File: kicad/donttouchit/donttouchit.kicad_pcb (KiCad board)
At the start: 2 copper layers, 40 x 61 mm, 46 parts, among them J1 Conn_01x02_Female, J10 Conn_01x04_Male, J2 Conn_01x02_Female, J3 Conn_01x02_Female, J4 Conn_01x02_Female, J5 Conn_01x02_Female, J6 Conn_01x02_Female, J7 Conn_01x02_Female, J8 Conn_01x02_Female, J9 Conn_01x02_Female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

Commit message: i2c pull up resistors added
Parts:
- added R1: 2k2, Resistor_SMD:R_0603_1608Metric_Pad0.98x0.95mm_HandSolder, F.Cu at (138.4, 77.3)
- added R2: 2k2, Resistor_SMD:R_0603_1608Metric_Pad0.98x0.95mm_HandSolder, F.Cu at (136.7, 77.3)
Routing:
- net Net-(J10-Pad2): track 3.26 -> 8.86 mm
- net VCC: track 19.9 -> 23.2 mm
- net Net-(J10-Pad3): track 16.9 -> 20.1 mm, vias 1 -> 2
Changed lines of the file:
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@@
   (net 7 "IN2B")
   (net 8 "IN2A")
-  (net 9 "Net-(U1-Pad5)")
+  (net 9 "Net-(TP15-Pad1)")
   (net 10 "Net-(U1-Pad3)")
   (net 11 "IN3B")
@@
       (net 2 "GND") (pinfunction "ADDR") (pintype "input"))
     (pad "5" smd roundrect (at -0.75 1.9375) (size 0.25 0.875) (layers "F.Cu" "F.Paste" "F.Mask") (roundrect_rratio 0.25)
-      (net 9 "Net-(U1-Pad5)") (pinfunction "INTB") (pintype "open_collector"))
+      (net 9 "Net-(TP15-Pad1)") (pinfunction "INTB") (pintype "open_collector"))
     (pad "6" smd roundrect (at -0.25 1.9375) (size 0.25 0.875) (layers "F.Cu" "F.Paste" "F.Mask") (roundrect_rratio 0.25)
       (net 2 "GND") (pinfunction "SD") (pintype "input"))
@@
       (net 11 "IN3B") (pinfunction "1") (pintype "passive"))
   )
+  (footprint "Resistor_SMD:R_0603_1608Metric_Pad0.98x0.95mm_HandSolder" (layer "F.Cu")
+    (at 136.7 77.3 90)
+    (descr "Resistor SMD 0603 (1608 Metric), square (rectangular) end terminal, IPC_7351 nominal with elongated pad for handsoldering. (Body size source: IPC-SM-782 page 72, https://www.pcb-3d.com/wordpress/wp-content/uploads/ipc-sm-782a_amendment_1_and_2.pdf), generated with kicad-footprint-generator")
+    (tags "resistor handsolder")
+    (property "Sheetfile" "donttouchit.kicad_sch")
+    (property "Sheetname" "")
+    (attr smd)
+    (fp_text reference "R2" (at 0 -1.43 90) (layer "F.SilkS")
+      (effects (font (size 1 1) (thickness 0.15)))
+    )
+    (fp_text value "2k2" (at 0 1.43 90) (layer "F.Fab")
+      (effects (font (size 1 1) (thickness 0.15)))
+    )
+    (fp_text user "${REFERENCE}" (at 0 0 90) (layer "F.Fab")
+      (effects (font (size 0.4 0.4) (thickness 0.06)))
+    )
+    (fp_line (start -0.254724 0.5225) (end 0.254724 0.5225) (layer "F.SilkS") (width 0.12))
+    (fp_line (start -0.254724 -0.5225) (end 0.254724 -0.5225) (layer "F.SilkS") (width 0.12))
+    (fp_line (start 1.65 -0.73) (end 1.65 0.73) (layer "F.CrtYd") (width 0.05))
+    (fp_line (start 1.65 0.73) (end -1.65 0.73) (layer "F.CrtYd") (width 0.05))
+    (fp_line (start -1.65 -0.73) (end 1.65 -0.73) (layer "F.CrtYd") (width 0.05))
+    (fp_line (start -1.65 0.73) (end -1.65 -0.73) (layer "F.CrtYd") (width 0.05))
+    (fp_line (start -0.8 -0.4125) (end 0.8 -0.4125) (layer "F.Fab") (width 0.1))
+    (fp_line (start 0.8 -0.4125) (end 0.8 0.4125) (layer "F.Fab") (width 0.1))
+    (fp_line (start -0.8 0.4125) (end -0.8 -0.4125) (layer "F.Fab") (width 0.1))
+    (fp_line (start 0.8 0.4125) (end -0.8 0.4125) (layer "F.Fab") (width 0.1))
+    (pad "1" smd roundrect (at -0.9125 0 90) (size 0.975 0.95) (layers "F.Cu" "F.Paste" "F.Mask") (roundrect_rratio 0.25)
+      (net 1 "VCC") (pintype "passive"))
+    (pad "2" smd roundrect (at 0.9125 0 90) (size 0.975 0.95) (layers "F.Cu" "F.Paste" "F.Mask") (roundrect_rratio 0.25)
+      (net 14 "Net-(J10-Pad3)") (pintype "passive"))
+    (model "${KICAD6_3DMODEL_DIR}/Resistor_SMD.3dshapes/R_0603_1608Metric.wrl"
+      (offset (xyz 0 0 0))
+      (scale (xyz 1 1 1))
+      (rotate (xyz 0 0 0))
+    )
+  )
   (footprint "TestPoint:TestPoint_THTPad_1.5x1.5mm_Drill0.7mm" (layer "F.Cu")
     (at 143 77)
@@
     (pad "1" thru_hole rect (at 0 0) (size 1.5 1.5) (drill 0.7) (layers *.Cu *.Mask)
       (net 3 "IN0B") (pinfunction "1") (pintype "passive"))
+  )
+  (footprint "Resistor_SMD:R_0603_1608Metric_Pad0.98x0.95mm_HandSolder" (layer "F.Cu")
+    (at 138.4 77.3 90)
+    (descr "Resistor SMD 0603 (1608 Metric), square (rectangular) end terminal, IPC_7351 nominal with elongated pad for handsoldering. (Body size source: IPC-SM-782 page 72, https://www.pcb-3d.com/wordpress/wp-content/uploads/ipc-sm-782a_amendment_1_and_2.pdf), generated with kicad-footprint-generator")
+    (tags "resistor handsolder")
+    (property "Sheetfile" "donttouchit.kicad_sch")
+    (property "Sheetname" "")
+    (attr smd)
+    (fp_text reference "R1" (at 0 -1.43 90) (layer "F.SilkS")
+      (effects (font (size 1 1) (thickness 0.15)))
+    )
+    (fp_text value "2k2" (at 0 1.43 90) (layer "F.Fab")
+      (effects (font (size 1 1) (thickness 0.15)))
+    )
+    (fp_text user "${REFERENCE}" (at 0 0 90) (layer "F.Fab")
+      (effects (font (size 0.4 0.4) (thickness 0.06)))
+    )
+    (fp_line (start -0.254724 0.5225) (end 0.254724 0.5225) (layer "F.SilkS") (width 0.12))
+    (fp_line (start -0.254724 -0.5225) (end 0.254724 -0.5225) (layer "F.SilkS") (width 0.12))
+    (fp_line (start -1.65 0.73) (end -1.65 -0.73) (layer "F.CrtYd") (width 0.05))
+    (fp_line (start -1.65 -0.73) (end 1.65 -0.73) (layer "F.CrtYd") (width 0.05))
+    (fp_line (start 1.65 -0.73) (end 1.65 0.73) (layer "F.CrtYd") (width 0.05))
+    (fp_line (start 1.65 0.73) (end -1.65 0.73) (layer "F.CrtYd") (width 0.05))
+    (fp_line (start 0.8 -0.4125) (end 0.8 0.4125) (layer "F.Fab") (width 0.1))
+    (fp_line (start -0.8 0.4125) (end -0.8 -0.4125) (layer "F.Fab") (width 0.1))
+    (fp_line (start 0.8 0.4125) (end -0.8 0.4125) (layer "F.Fab") (width 0.1))
+    (fp_line (start -0.8 -0.4125) (end 0.8 -0.4125) (layer "F.Fab") (width 0.1))
+    (pad "1" smd roundrect (at -0.9125 0 90) (size 0.975 0.95) (layers "F.Cu" "F.Paste" "F.Mask") (roundrect_rratio 0.25)
+      (net 1 "VCC") (pintype "passive"))
+    (pad "2" smd roundrect (at 0.9125 0 90) (size 0.975 0.95) (layers "F.Cu" "F.Paste" "F.Mask") (roundrect_rratio 0.25)
+      (net 13 "Net-(J10-Pad2)") (pintype "passive"))
+    (model "${KICAD6_3DMODEL_DIR}/Resistor_SMD.3dshapes/R_0603_1608Metric.wrl"
+      (offset (xyz 0 0 0))
+      (scale (xyz 1 1 1))
+      (rotate (xyz 0 0 0))
+    )
   )
   (footprint "TestPoint:TestPoint_THTPad_1.5x1.5mm_Drill0.7mm" (layer "F.Cu")
@@
     (fp_line (start 1.25 -1.25) (end 1.25 1.25) (layer "B.CrtYd") (width 0.05))
     (pad "1" thru_hole rect (at 0 0 180) (size 1.5 1.5) (drill 0.7) (layers *.Cu *.Mask)
-      (net 9 "Net-(U1-Pad5)") (pinfunction "1") (pintype "passive"))
+      (net 9 "Net-(TP15-Pad1)") (pinfunction "1") (pintype "passive"))
   )
   (footprint "Library:PCBConnPads" (layer "B.Cu")
@@
   (segment (start 136.75 83) (end 136.75 81) (width 0.5) (layer "F.Cu") (net 1))
   (segment (start 137.5 80.25) (end 137.5 80.75) (width 0.5) (layer "F.Cu") (net 1))
+  (segment (start 138.4 78.2125) (end 136.7 78.2125) (width 0.5) (layer "F.Cu") (net 1))
   (segment (start 138.325 82.975) (end 136.775 82.975) (width 0.127) (layer "F.Cu") (net 1))
+  (segment (start 138.3875 79.75) (end 138.3875 78.225) (width 0.5) (layer "F.Cu") (net 1))
   (segment (start 144.1 82.7875) (end 144.1 84.2375) (width 0.25) (layer "F.Cu") (net 1))
+  (segment (start 138.3875 78.225) (end 138.4 78.2125) (width 0.5) (layer "F.Cu") (net 1))
   (segment (start 142.75 84.3875) (end 144.25 84.3875) (width 0.5) (layer "F.Cu") (net 1))
   (segment (start 137.5 80.75) (end 138.25 80.75) (width 0.5) (layer "F.Cu") (net 1))
@@
   (segment (start 143.6 78.9125) (end 143.6 77.6) (width 0.25) (layer "F.Cu") (net 12))
   (segment (start 141.1 80.6) (end 141 80.5) (width 0.25) (layer "F.Cu") (net 13))
+  (segment (start 139.2 78.1) (end 139.2 77.1875) (width 0.25) (layer "F.Cu") (net 13))
+  (segment (start 140.2 78.4) (end 139.5 78.4) (width 0.25) (layer "F.Cu") (net 13))
+  (segment (start 141 80.5) (end 141 79.2) (width 0.25) (layer "F.Cu") (net 13))
   (segment (start 141.9125 80.6) (end 141.1 80.6) (width 0.25) (layer "F.Cu") (net 13))
+  (segment (start 139.5 78.4) (end 139.2 78.1) (width 0.25) (layer "F.Cu") (net 13))
+  (segment (start 141 79.2) (end 140.2 78.4) (width 0.25) (layer "F.Cu") (net 13))
+  (segment (start 139.2 77.1875) (end 138.4 76.3875) (width 0.25) (layer "F.Cu") (net 13))
   (via (at 141 80.5) (size 0.6) (drill 0.3) (layers "F.Cu" "B.Cu") (free) (net 13))
   (segment (start 141 80.5) (end 140.25 81.25) (width 0.25) (layer "B.Cu") (net 13))
   (segment (start 140.25 81.25) (end 139 81.25) (width 0.25) (layer "B.Cu") (net 13))
   (segment (start 141.9125 80.1) (end 141.9125 79.3375) (width 0.25) (layer "F.Cu") (net 14))
+  (segment (start 135.25 77.8375) (end 136.7 76.3875) (width 0.25) (layer "F.Cu") (net 14))
+  (segment (start 135.25 79) (end 135.25 77.8375) (width 0.25) (layer "F.Cu") (net 14))
   (segment (start 141.9125 79.3375) (end 142.25 79) (width 0.25) (layer "F.Cu") (net 14))
+  (via (at 135.25 79) (size 0.6) (drill 0.3) (layers "F.Cu" "B.Cu") (net 14))
   (via (at 142.25 79) (size 0.6) (drill 0.3) (layers "F.Cu" "B.Cu") (free) (net 14))
   (segment (start 135.25 82.75) (end 135.75 83.25) (width 0.25) (layer "B.Cu") (net 14))

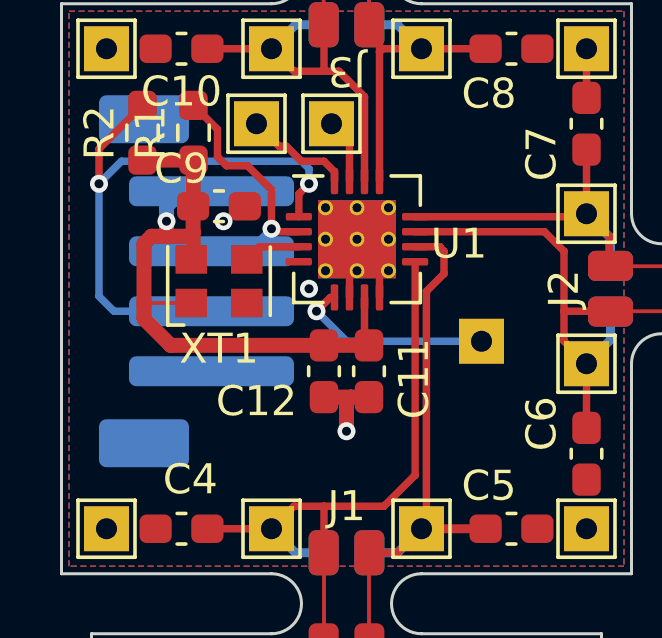
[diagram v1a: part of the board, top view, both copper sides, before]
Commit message: temperature sensor added
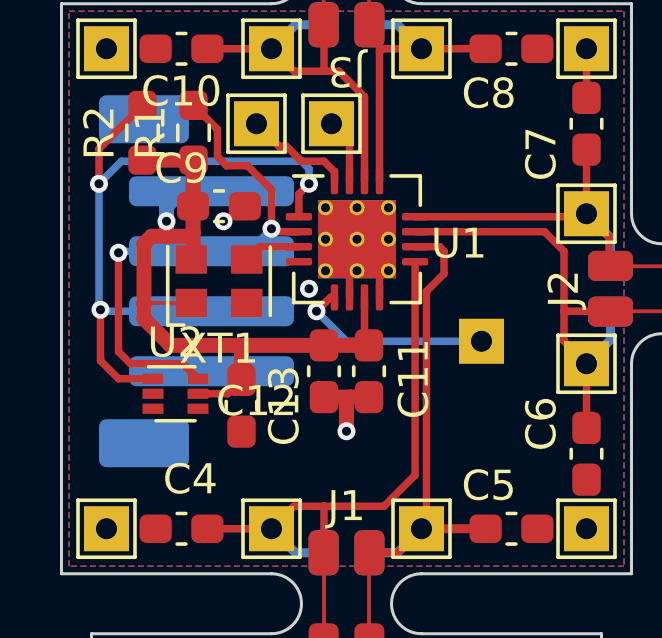
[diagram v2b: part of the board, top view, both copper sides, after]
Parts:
- added C13: 100n, Capacitor_SMD:C_0603_1608Metric_Pad1.08x0.95mm_HandSolder, F.Cu at (140.0, 86.4)
- added U2: TMP112xxDRL, Package_TO_SOT_SMD:SOT-563, F.Cu at (137.8, 86.0)
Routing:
- net Net-(J10-Pin_2): track 8.86 -> 18.3 mm, vias 1 -> 2
- net Net-(J10-Pin_3): track 20.1 -> 24.0 mm, vias 2 -> 3
- net VCC: track 23.2 -> 26.0 mm

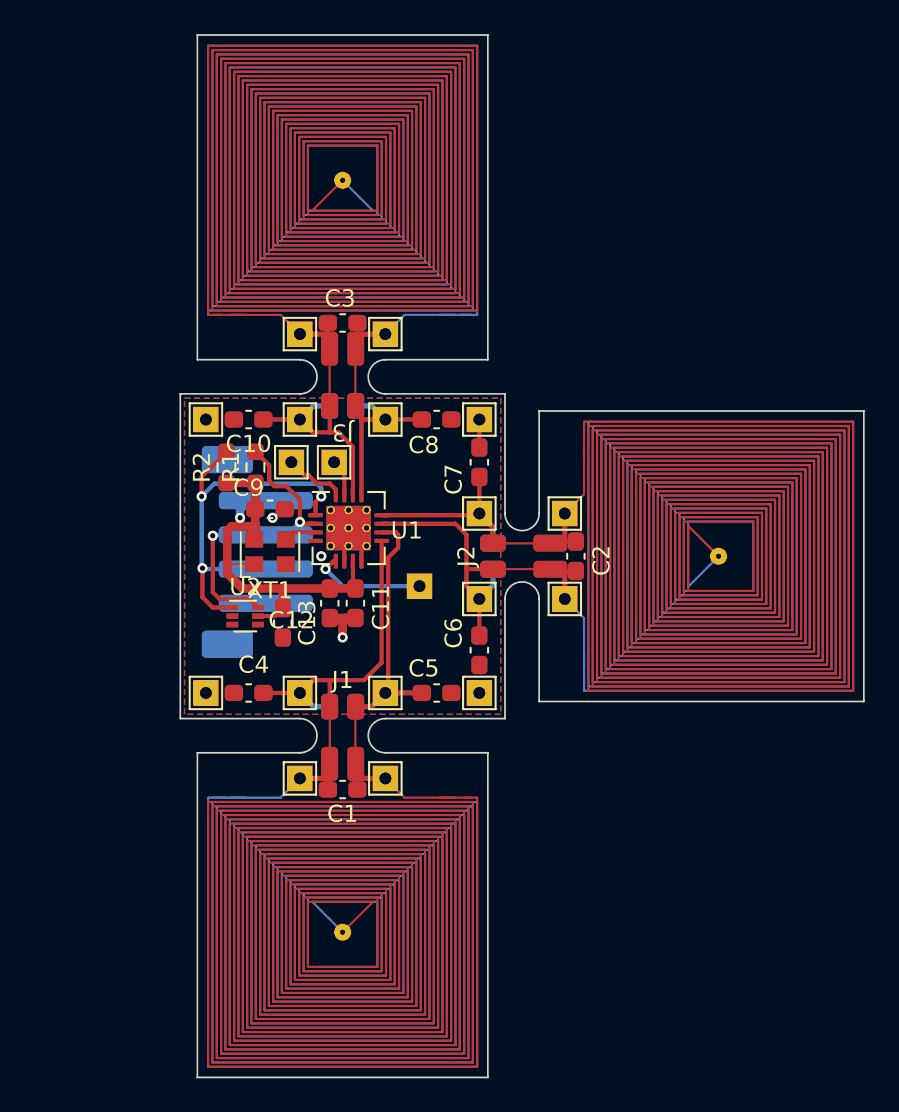
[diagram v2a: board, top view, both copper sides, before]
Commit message: I2C address solderbridges added / mounting hole added / size reduced for control section
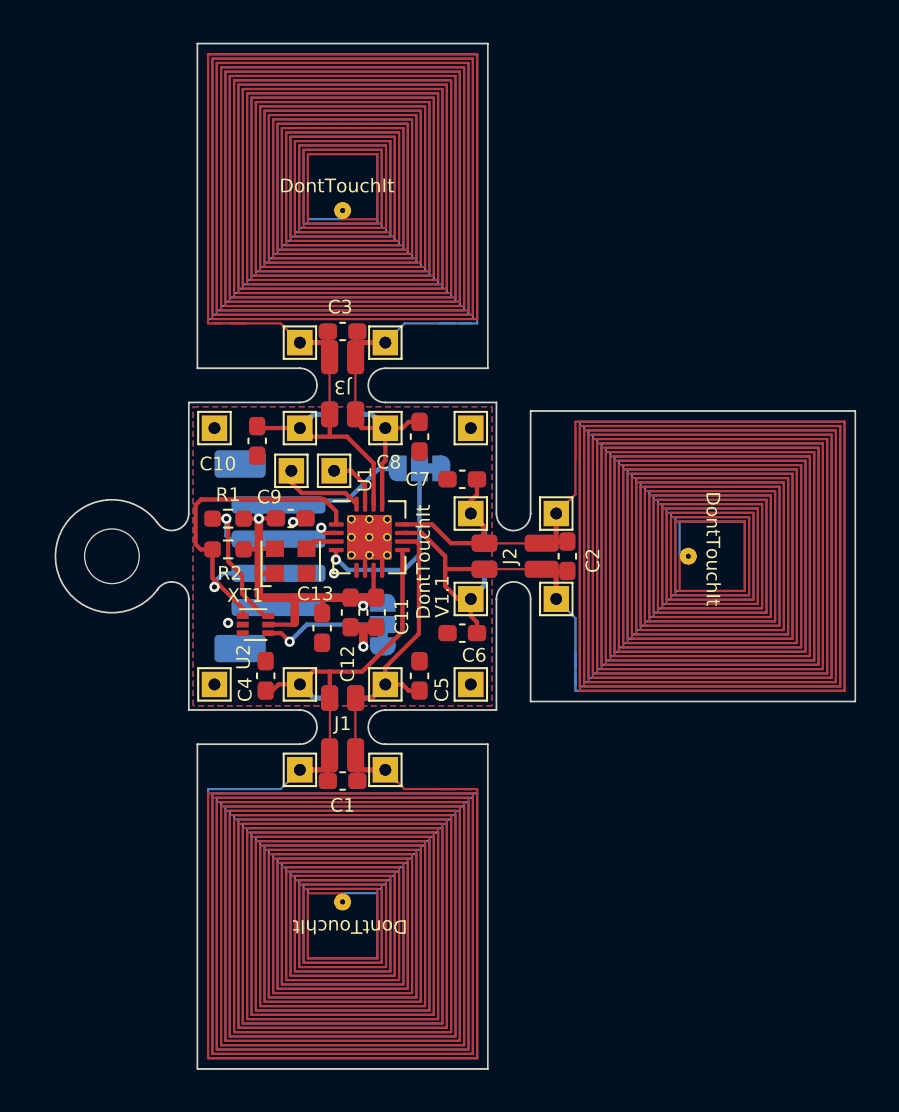
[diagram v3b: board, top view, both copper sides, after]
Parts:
- removed TP15: TestPoint, TestPoint:TestPoint_THTPad_1.5x1.5mm_Drill0.7mm
- added H1: MountingHole, MountingHole:MountingHole_3.2mm_M3, F.Cu at (126.8, 82.6)
- added JP1: I2C Adress Select, Jumper:SolderJumper-3_P1.3mm_Bridged12_RoundedPad1.0x1.5mm, B.Cu at (145.8, 86.5)
- added JP2: I2C Adress Select, Jumper:SolderJumper-3_P1.3mm_Bridged12_RoundedPad1.0x1.5mm, B.Cu at (148.0, 77.4)
- moved R2 4.80 mm to (136.8, 82.1), turned to 180 degrees
- moved R1 3.40 mm to (136.8, 80.3), turned to 180 degrees
- moved C13 2.32 mm to (142.3, 86.7)
- moved C4 1.41 mm to (139.0, 89.5), turned to 90 degrees
- moved C5 1.41 mm to (148.0, 89.5), turned to 90 degrees
- moved C6 1.41 mm to (150.5, 87.0), turned to 180 degrees
- moved C7 1.41 mm to (150.5, 78.0), turned to 180 degrees
- moved C8 1.41 mm to (148.0, 75.5), turned to -90 degrees
- moved C10 1.35 mm to (138.5, 75.8), turned to -90 degrees
- moved U1 1.33 mm to (145.1, 81.4)
- moved C11 1.33 mm to (145.5, 85.8)
- moved C12 1.33 mm to (144.0, 85.8)
- moved C9 1.33 mm to (140.5, 80.3)
- moved XT1 1.33 mm to (140.5, 82.8)
- moved J10 0.79 mm to (139.2, 82.5)
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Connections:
- U1 pad 4: GND -> Net-(JP2-C)
- U1 pad 5: Net-(U1-INTB) -> unconnected-(U1-INTB-Pad5)
- U2 pad 4: GND -> Net-(JP1-C)
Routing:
- net Net-(JP2-C): track 0.00 -> 11.1 mm, vias 0 -> 1
- net Net-(JP1-C): track 0.00 -> 7.31 mm, vias 0 -> 1
- net VCC: track 26.0 -> 33.1 mm, vias 1 -> 2
- net Net-(U1-INTB): track 6.71 -> 0.00 mm, vias 1 -> 0
- net Net-(J10-Pin_2): track 18.3 -> 15.6 mm
- net Net-(J10-Pin_3): track 24.0 -> 22.0 mm, vias 3 -> 1
- net IN1A: track 27.1 -> 25.2 mm
- net GND: track 8.76 -> 7.12 mm, vias 3 -> 4
- net IN3B: track 3.58 -> 5.03 mm
- net IN2B: track 25.0 -> 26.1 mm
- net IN3A: track 2.16 -> 3.29 mm
- net IN0A: track 30.6 -> 30.0 mm
- net IN0B: track 28.3 -> 27.8 mm
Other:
- board size 40 x 61 mm -> 46.8 x 60 mm
- board text added: "0x2A"
- board text added: "0x2B"
- board text added: "0x48"
- board text added: "0x49"
- board text added: "3V3"
- board text added: "DontTouchIt"
- board text added: "Gnd"
- board text added: "LDC"
- board text added: "SCL"
- board text added: "SDA"
- board text added: "Temp"
- board text added: "V1.1"

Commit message: smaller formfactor that fits in the space of an Omron probe, 4th sensor pads removed
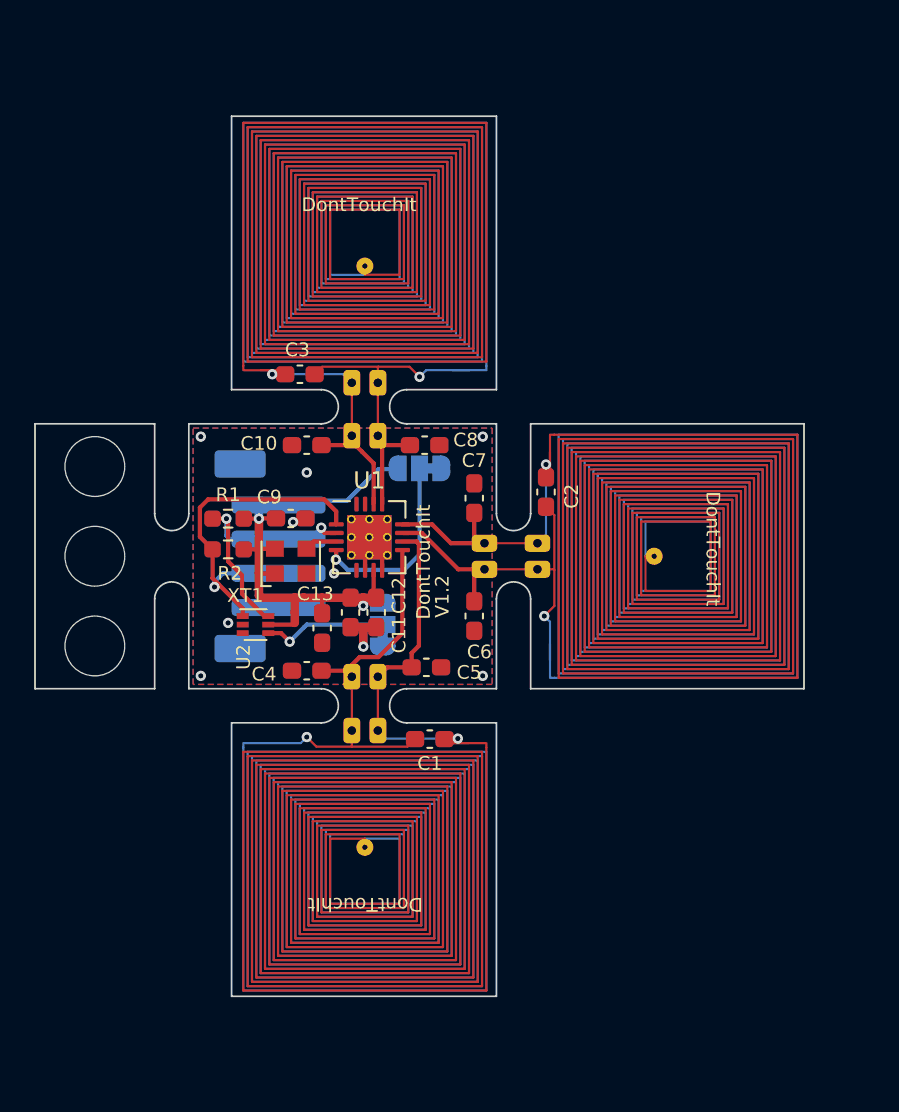
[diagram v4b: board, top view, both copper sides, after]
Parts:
- removed J4, J5, J6: Conn_01x02_Female, Library:PCBConnPads
- removed TP1, TP10, TP11, TP12, TP13, TP14, TP16, TP17, TP18, TP19, TP2, TP3, TP4, TP5, TP6, TP7, TP8, TP9: TestPoint, TestPoint:TestPoint_THTPad_1.5x1.5mm_Drill0.7mm
- added H2: MountingHole, MountingHole:MountingHole_3.5mm, F.Cu at (114.1, 85.9)
- added H3: MountingHole, MountingHole:MountingHole_3.5mm, F.Cu at (128.1, 82.9)
- H1: footprint MountingHole:MountingHole_3.2mm_M3 -> MountingHole:MountingHole_3.5mm
- J1, J2, J3: footprint Library:PCBConnPads -> Library:PCBConnPadsTHT
- J7, J8, J9: footprint Library:PCBConnPadsLong -> Library:PCBConnPadsTHT
- L1, L2, L3: footprint Library:Coil -> Library:Coil_14x14
- U1: footprint Package_DFN_QFN:WQFN-16-1EP_4x4mm_P0.5mm_EP2.6x2.6mm_ThermalVias -> Library:WQFN-16-1EP_4x4mm_P0.5mm_EP2.6x2.6mm_ThermalVias
- moved H1 13.8 mm to (114.1, 77.3)
- moved C1 5.66 mm to (148.6, 93.2)
- moved C2 3.96 mm to (155.4, 78.7)
- moved C3 3.54 mm to (141.0, 71.8)
- moved L3 3.50 mm to (144.8, 64.2)
- moved L1 3.45 mm to (144.8, 100.8)
- moved C10 2.91 mm to (141.4, 76.0), turned to 180 degrees
- moved C4 2.42 mm to (141.4, 89.2), turned to 180 degrees
- moved L2 2.00 mm to (163.0, 82.5)
- moved J9 1.98 mm to (144.8, 72.3)
- moved J7 1.95 mm to (144.8, 92.7)
- moved J1 1.80 mm to (144.8, 89.5)
- moved J3 1.80 mm to (144.8, 75.5)
- moved C7 1.30 mm to (151.2, 79.1), turned to 90 degrees
- moved C6 1.22 mm to (151.2, 86.0), turned to -90 degrees
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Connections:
- U1 pad 15: IN3A -> unconnected-(U1-IN3A-Pad15)
- U1 pad 16: IN3B -> unconnected-(U1-IN3B-Pad16)
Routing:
- net IN2B: track 26.1 -> 16.7 mm, vias 0 -> 1
- net IN0B: track 27.8 -> 21.0 mm, vias 0 -> 1
- net IN1B: track 23.3 -> 17.9 mm, vias 0 -> 1
- net IN0A: track 30.0 -> 24.9 mm, vias 0 -> 1
- net IN3B: track 5.03 -> 0.00 mm
- net IN2A: track 23.9 -> 19.4 mm, vias 0 -> 1
- net IN1A: track 25.2 -> 21.8 mm, vias 0 -> 1
- net IN3A: track 3.29 -> 0.00 mm
- net Net-(J10-Pin_3): track 22.0 -> 21.2 mm
- net GND: vias 4 -> 9
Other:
- board size 46.8 x 60 mm -> 45 x 51.5 mm
- board text added: "V1.2"
- board text removed: "V1.1"
